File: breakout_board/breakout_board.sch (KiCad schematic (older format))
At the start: 57 parts

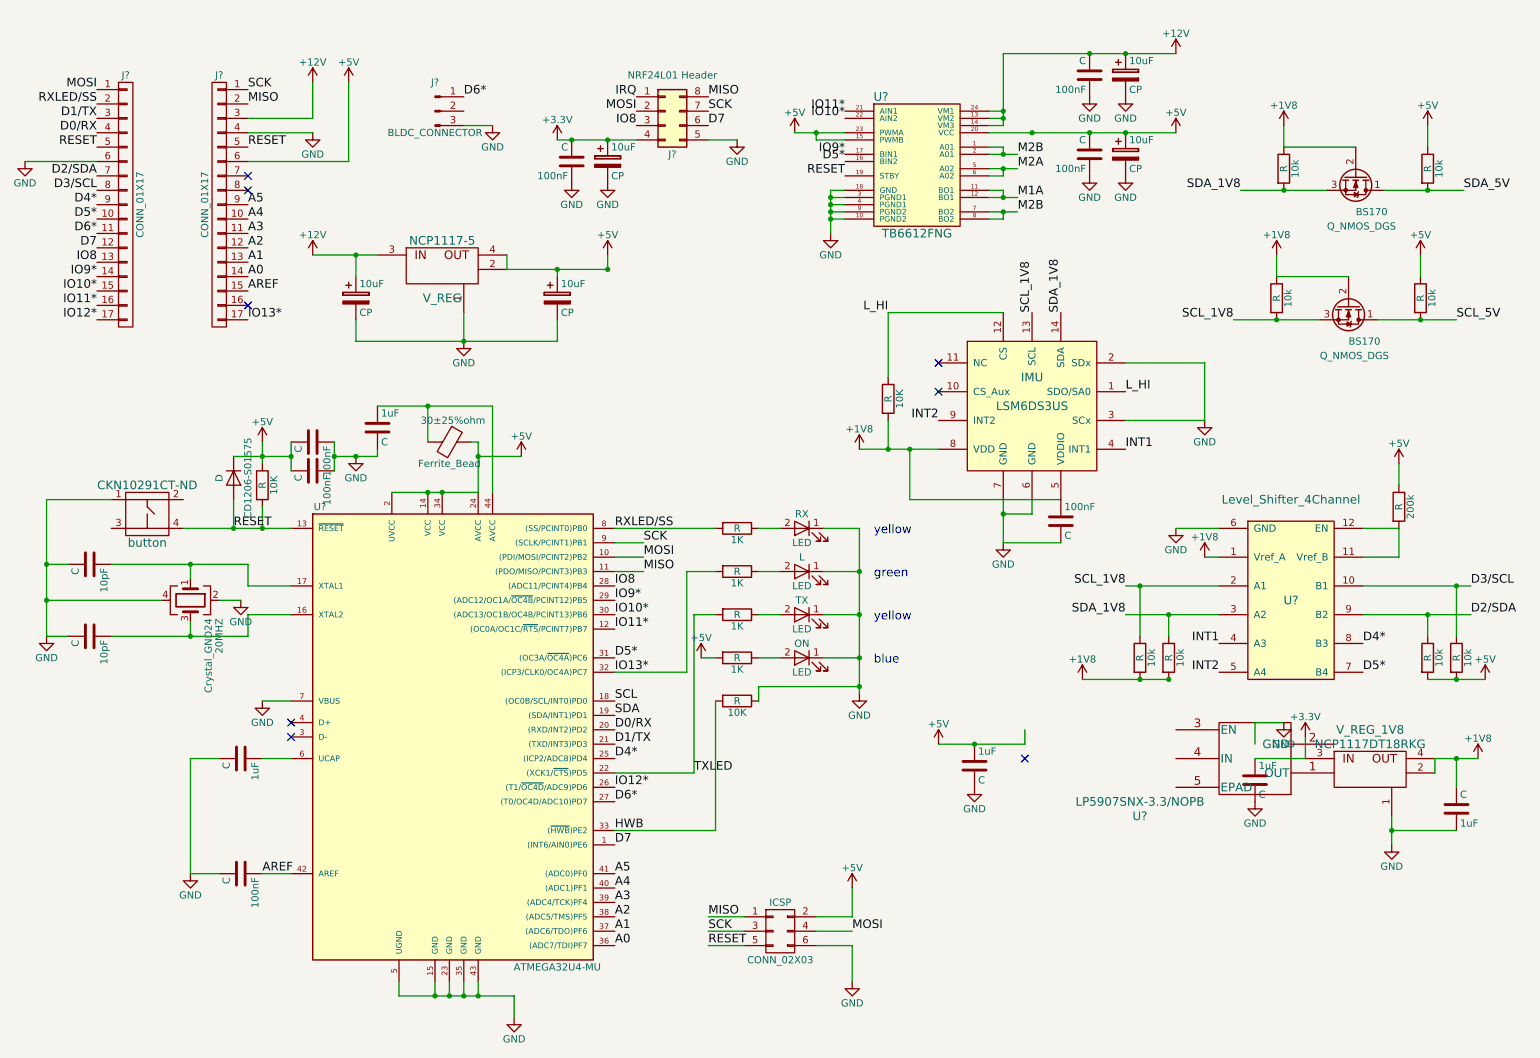
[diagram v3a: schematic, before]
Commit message: Fixed trash labeling and remade ugly garbage while changing capacitors and resistors to be correct
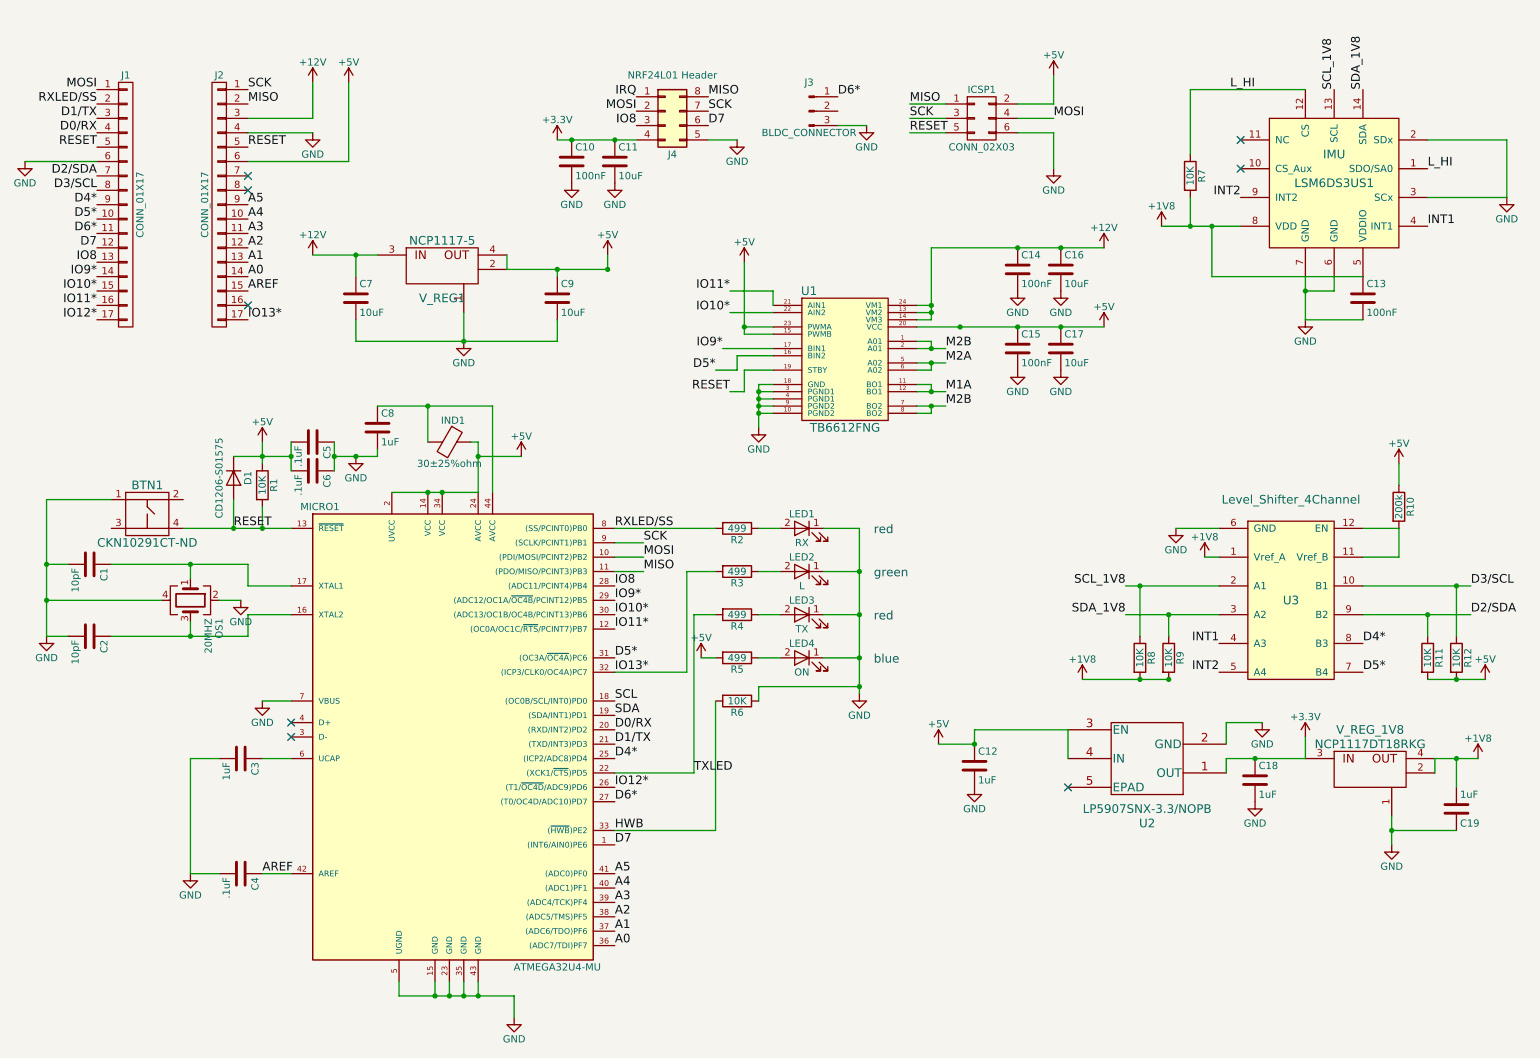
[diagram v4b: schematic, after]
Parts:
- removed 10k (x4): R, symbol R
- removed 10uF (x5): CP, symbol CP
- removed BS170 (x2): Q_NMOS_DGS, symbol Q_NMOS_DGS
- added C11, C16, C17, C7, C9: 10uF, symbol C
- BTN1: renamed from CKN10291CT-ND; value button -> CKN10291CT-ND
- C1, C2: renamed from 10pF; value C -> 10pF
- C10, C13, C14, C15: renamed from 100nF; value C -> 100nF
- C12, C18, C19, C3, C8: renamed from 1uF; value C -> 1uF
- C4, C5, C6: renamed from 100nF; value C -> .1uF
- D1: renamed from CD1206-S01575; value D -> CD1206-S01575
- IND1: renamed from 30±25%ohm; value Ferrite_Bead -> 30±25%ohm
- LED1: renamed from RX; value LED -> RX; Color (none) -> Red
- LED2: renamed from L; value LED -> L; Color (none) -> Green
- LED3: renamed from TX; value LED -> TX; Color (none) -> Red
- LED4: renamed from ON; value LED -> ON; Color (none) -> Blue
- OS1: renamed from 20MHZ; value Crystal_GND24 -> 20MHZ
- R1, R6, R7: renamed from 10K; value R -> 10K
- R10: renamed from 200k; value R -> 200k
- R11, R12, R8, R9: renamed from 10k; value R -> 10K
- R2, R3, R4, R5: renamed from 1K; value R -> 499
- gave numbers to parts that had none: 8
- renumbered ICSP to ICSP1, LSM6DS3US to LSM6DS3US1, V_REG to V_REG1
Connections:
- net +12V: now also C14.1, C16.1, C7.1; no longer C14.2
- net +3V3: now also C10.1, U2.1 (OUT), C11.1; no longer C10.2
- net +5V: now also C15.1, U2.3 (EN), U2.4 (IN), C17.1, C9.1; no longer C15.2
- net GND: now also C10.2, C14.2, C15.2, U2.2 (GND), C11.2, C16.2, C17.2, C7.2, C9.2; no longer C10.1, C14.1, C15.1
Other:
- note added: "red"
- note removed: "yellow"
- moved on the sheet: C13, C14, C15, ICSP1, J3, LSM6DS3US1, R7, U1, U2

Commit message: Added submission files
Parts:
- removed J3: BLDC_CONNECTOR, Connectors:PINHEAD1-3, symbol Conn_01x03_Male
- added J?: CONN_01X03, symbol CONN_01X03
- J4: value NRF24L01 Header -> CONN_02x04
- U3: value Level_Shifter_4Channel -> LSF0204RUTR
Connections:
- net D4*: no longer J1.9 (P9)
- net D5*: no longer J1.10 (P10), U1.16 (BIN2)
- net D6*: now also U1.16 (BIN2), J?.3 (P3); no longer J1.11 (P11)
- net GND: now also J?.1 (P1)
- no-connect marks 8 -> 12
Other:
- note added: "1V8 REGULATOR"
- note added: "3V3 REGULATOR"
- note added: "5V REGULATOR"
- note added: "BLDC HEADER"
- note added: "BREAKOUT HEADER PINS"
- note added: "DC MOTOR CONTROLLER"
- note added: "ICSP HEADER"
- note added: "IMU"
- note added: "LEVEL SHIFTER"
- note added: "MICROCONTROLLER"
- note added: "NRF24L01 HEADER"
- moved on the sheet: C10, C11, C13, C14, C15, C16, C17, C7, C9, ICSP1, J4, LSM6DS3US1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

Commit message: Made changes from Brad
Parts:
- removed R10: 200k, symbol R
- added R? (x2): 10K, symbol R
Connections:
- net +5V: now also U3.11 (Vref_B), U3.12 (EN), R?.2, R?.2
- net D4*: now also R?.1
- net D5*: now also R?.1
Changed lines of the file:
@@
 SCL_1V8
 $Comp
-L R R10
-U 1 1 59D06871
+L +5V #PWR024
+U 1 1 59D0692F
 P 10150 2900
-F 0 "R10" V 10230 2900 50  0000 C CNN
-F 1 "200k" V 10150 2900 50  0000 C CNN
-F 2 "" V 10080 2900 50  0001 C CNN
+F 0 "#PWR024" H 10150 2750 50  0001 C CNN
+F 1 "+5V" H 10150 3040 50  0000 C CNN
+F 2 "" H 10150 2900 50  0001 C CNN
 F 3 "" H 10150 2900 50  0001 C CNN
 	1    10150 2900
-	1    0    0    -1
-$EndComp
-$Comp
-L +5V #PWR024
-U 1 1 59D0692F
-P 10150 2600
-F 0 "#PWR024" H 10150 2450 50  0001 C CNN
-F 1 "+5V" H 10150 2740 50  0000 C CNN
-F 2 "" H 10150 2600 50  0001 C CNN
-F 3 "" H 10150 2600 50  0001 C CNN
-	1    10150 2600
 	1    0    0    -1
 $EndComp
@@
 	1    0    0    -1
 $EndComp
-Text Label 9900 3850 0    60   ~ 0
+Text Label 10100 3850 0    60   ~ 0
 D4*
 Text Label 9900 4050 0    60   ~ 0
@@
 	10150 3050 9900 3050
 Wire Wire Line
-	10150 2750 10150 2600
+	10150 3050 10150 2900
 Wire Wire Line
 	8500 2550 8900 2550
@@
 	10350 4100 10550 4100
 Wire Wire Line
-	10550 4100 10750 4100
+	10550 4100 10650 4100
+Wire Wire Line
+	10650 4100 10750 4100
 Connection ~ 10550 4100
 Wire Wire Line
@@
 NoConn ~ 1200 1950
 NoConn ~ 1200 2050
+$Comp
+L R R?
+U 1 1 59D693C3
+P 9900 4300
+F 0 "R?" V 9980 4300 50  0000 C CNN
+F 1 "10K" V 9900 4300 50  0000 C CNN
+F 2 "" V 9830 4300 50  0001 C CNN
+F 3 "" H 9900 4300 50  0001 C CNN
+	1    9900 4300
+	1    0    0    -1
+$EndComp
+$Comp
+L R R?
+U 1 1 59D694D3
+P 10100 4300
+F 0 "R?" V 10180 4300 50  0000 C CNN
+F 1 "10K" V 10100 4300 50  0000 C CNN
+F 2 "" V 10030 4300 50  0001 C CNN
+F 3 "" H 10100 4300 50  0001 C CNN
+	1    10100 4300
+	1    0    0    -1
+$EndComp
+Wire Wire Line
+	9900 4050 9900 4150
+Wire Wire Line
+	9900 3850 10100 3850
+Wire Wire Line
+	10100 3850 10100 4150
+Wire Wire Line
+	10100 4450 10550 4450
+Wire Wire Line
+	10550 4450 10550 4100
+Wire Wire Line
+	9900 4450 9900 4550
+Wire Wire Line
+	9900 4550 10650 4550
+Wire Wire Line
+	10650 4550 10650 4100
+Connection ~ 10650 4100
 $EndSCHEMATC

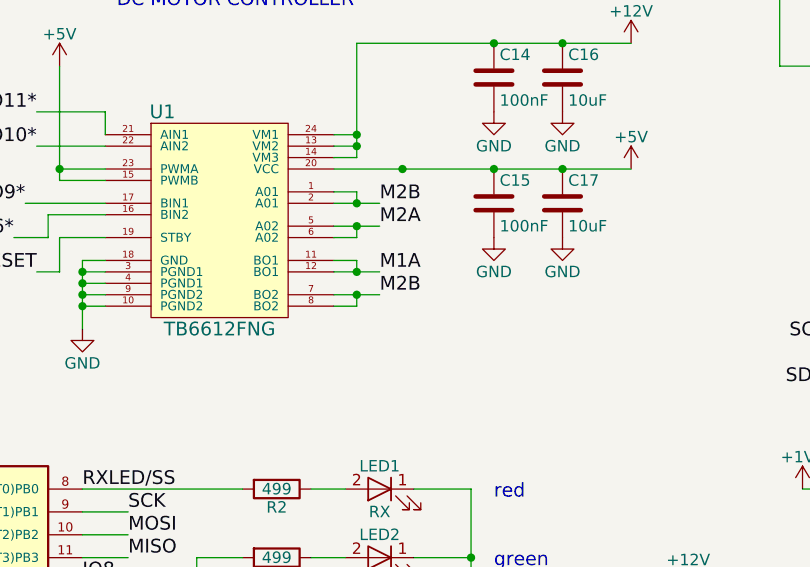
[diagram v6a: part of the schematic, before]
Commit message: Made some footprints
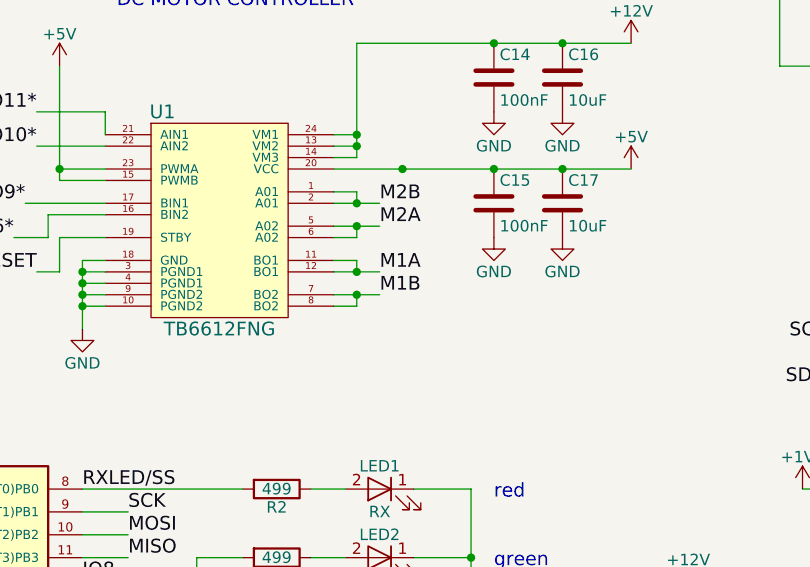
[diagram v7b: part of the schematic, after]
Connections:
- net M2B: no longer U1.7 (BO2), U1.8 (BO2)
- new net M1B: U1.7 (BO2), U1.8 (BO2)
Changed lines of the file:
@@
 M1A
 Text Label 6100 3250 0    60   ~ 0
-M2B
+M1B
 $Comp
 L GND #PWR030

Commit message: Footprinting done - needs checking.
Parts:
- BTN1: footprint (none) -> footprints:KMT071_NGJ_LHS
- C1, C10, C12, C13, C14, C15, C18, C19, C2, C3, C4, C5, C6, C8: footprint (none) -> Capacitors_SMD:C_0603
- C11, C16, C17, C7, C9: footprint (none) -> Capacitors_SMD:C_0805
- D1: footprint (none) -> Capacitors_SMD:C_0402
- ICSP1: footprint (none) -> Pin_Headers:Pin_Header_Straight_2x03_Pitch2.54mm
- IND1: footprint (none) -> Inductors_SMD:L_0805
- J1, J2: footprint (none) -> Pin_Headers:Pin_Header_Straight_1x14_Pitch2.54mm
- J3: renamed from J?; footprint (none) -> Pin_Headers:Pin_Header_Straight_1x03_Pitch2.54mm
- J4: footprint (none) -> Pin_Headers:Pin_Header_Straight_2x03_Pitch2.54mm_SMD
- LED1, LED2, LED3, LED4: footprint (none) -> LEDs:LED_0805
- LSM6DS3US1: footprint (none) -> footprints:LGA-14L
- MICRO1: footprint QFN44 -> footprints:ATMEGA32U4-MUR
- OS1: footprint (none) -> footprints:ABM11AIG
- R1, R11, R12, R2, R3, R4, R5, R6, R7, R8, R9: footprint (none) -> Resistors_SMD:R_0603
- R10, R13: renamed from R?; footprint (none) -> Resistors_SMD:R_0603
- U1: footprint (none) -> footprints:SOP65P760X160-24N
- U2: footprint DQN4 -> footprints:DQN4
- U3: footprint (none) -> footprints:R-PUQFN-N12
- V_REG1: footprint (none) -> footprints:NCP1117
- V_REG_1V8: footprint (none) -> footprints:TO229P990X238-4N
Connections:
- net +5V: no longer U3.12 (EN)
